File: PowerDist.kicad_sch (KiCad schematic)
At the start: 17 parts, among them J18 PowerConn, Q2 IRLML0030, U12 RI3-1205S, U13 NCP1117-3.3_SOT223

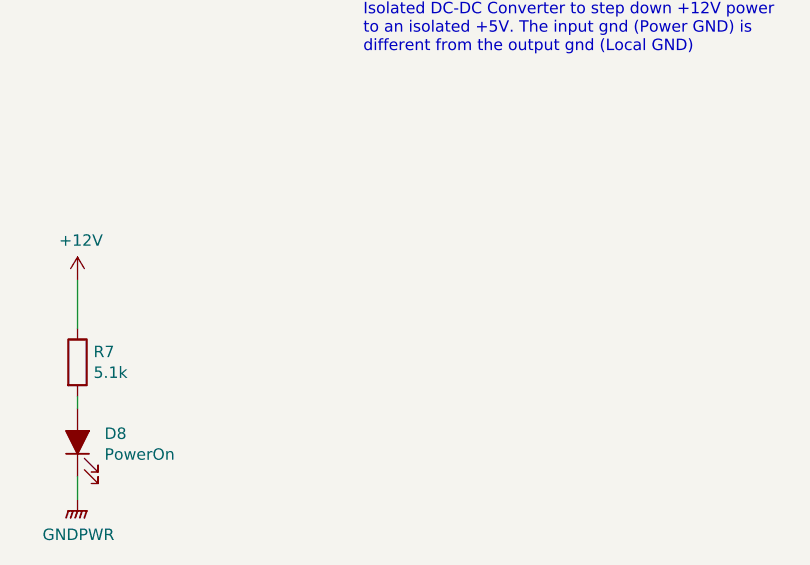
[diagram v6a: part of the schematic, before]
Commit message: Added 3A fuse to lights (estimated 9 lights, ~1.8 A plus buffer, changed fuse datasheet to match part number.
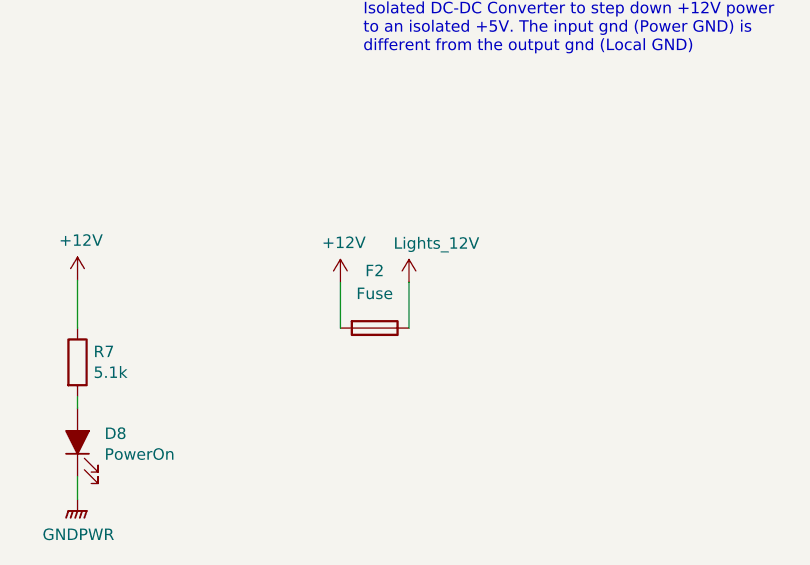
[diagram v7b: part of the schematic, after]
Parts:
- added F2: Fuse, Fuse:Fuse_1206_3216Metric, symbol Device:Fuse
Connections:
- net +12V: now also F2.2
- new net Lights_12V: F2.1
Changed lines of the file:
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@@
+	(wire
+		(pts
+			(xy 96.52 142.24) (xy 96.52 147.32)
+		)
+		(stroke
+			(width 0)
+			(type default)
+		)
+	)
 	(wire
 		(pts
@@
 		(pts
 			(xy 99.06 85.09) (xy 101.6 85.09)
+		)
+		(stroke
+			(width 0)
+			(type default)
+		)
+	)
+	(wire
+		(pts
+			(xy 88.9 142.24) (xy 88.9 147.32)
 		)
 		(stroke
@@
 	)
 	(symbol
+		(lib_id "power:+12V")
+		(at 88.9 142.24 0)
+		(unit 1)
+		(exclude_from_sim no)
+		(in_bom yes)
+		(on_board yes)
+		(dnp no)
+		(property "Reference" "#PWR035"
+			(at 88.9 146.05 0)
+			(effects
+				(font
+					(size 1.27 1.27)
+				)
+				(hide yes)
+			)
+		)
+		(property "Value" "+12V"
+			(at 89.281 137.8458 0)
+			(effects
+				(font
+					(size 1.27 1.27)
+				)
+			)
+		)
+		(property "Footprint" ""
+			(at 88.9 142.24 0)
+			(effects
+				(font
+					(size 1.27 1.27)
+				)
+				(hide yes)
+			)
+		)
+		(property "Datasheet" ""
+			(at 88.9 142.24 0)
+			(effects
+				(font
+					(size 1.27 1.27)
+				)
+				(hide yes)
+			)
+		)
+		(property "Description" "Power symbol creates a global label with name \"+12V\""
+			(at 88.9 142.24 0)
+			(effects
+				(font
+					(size 1.27 1.27)
+				)
+				(hide yes)
+			)
+		)
+		(pin "1"
+		)
+		(instances
+			(project "Controls-Leader"
+				(path "/66218487-e316-4467-9eba-79d4626ab24e/00000000-0000-0000-0000-00005f19a9c5"
+					(reference "#PWR035")
+					(unit 1)
+				)
+			)
+		)
+	)
+	(symbol
 		(lib_id "Diode:SD12_SOD323")
 		(at 55.88 82.55 90)
@@
 				(path "/66218487-e316-4467-9eba-79d4626ab24e/00000000-0000-0000-0000-00005f19a9c5"
 					(reference "TP9")
+					(unit 1)
+				)
+			)
+		)
+	)
+	(symbol
+		(lib_id "Device:Fuse")
+		(at 92.71 147.32 270)
+		(unit 1)
+		(exclude_from_sim no)
+		(in_bom yes)
+		(on_board yes)
+		(dnp no)
+		(fields_autoplaced yes)
+		(property "Reference" "F2"
+			(at 92.71 140.97 90)
+			(effects
+				(font
+					(size 1.27 1.27)
+				)
+			)
+		)
+		(property "Value" "Fuse"
+			(at 92.71 143.51 90)
+			(effects
+				(font
+					(size 1.27 1.27)
+				)
+			)
+		)
+		(property "Footprint" "Fuse:Fuse_1206_3216Metric"
+			(at 92.71 145.542 90)
+			(effects
+				(font
+					(size 1.27 1.27)
+				)
+				(hide yes)
+			)
+		)
+		(property "Datasheet" "https://cdn1-originals.webdamdb.com/14154_151726252?cache=1732578703&response-content-disposition=inline;filename=Littelfuse_Fuse_440_Datasheet.pdf&response-content-type=application/pdf&Policy=eyJTdGF0ZW1lbnQiOlt7IlJlc291cmNlIjoiaHR0cCo6Ly9jZG4xLW9yaWdpbmFscy53ZWJkYW1kYi5jb20vMTQxNTRfMTUxNzI2MjUyP2NhY2hlPTE3MzI1Nzg3MDMmcmVzcG9uc2UtY29udGVudC1kaXNwb3NpdGlvbj1pbmxpbmU7ZmlsZW5hbWU9TGl0dGVsZnVzZV9GdXNlXzQ0MF9EYXRhc2hlZXQucGRmJnJlc3BvbnNlLWNvbnRlbnQtdHlwZT1hcHBsaWNhdGlvbi9wZGYiLCJDb25kaXRpb24iOnsiRGF0ZUxlc3NUaGFuIjp7IkFXUzpFcG9jaFRpbWUiOjIxNDc0MTQ0MDB9fX1dfQ__&Signature=LvuAwZFRA50GgO3enXap8HKIUGPX5c5rkh5wZKPs26l6wVeoa4e3HlPw3JGKu2XLN2mZjekZmdxpYAqdsOFkELgudMCZJJtLLB7CYjilNx-uV0W3LH-UU7j3-UHutrdbGZC827tk~6zJnsDB2xvB98cGEExGU7KZGJANC28jW8XIJPT4hhWJZ3P8A6kmskdfDQHTby0fQLrBki0Cy~JqgrzKU3pon-XdzROvTXY9QwTk8wFP1CPSyVTSOLlxVTny3kR~8QXaPjArNl9XYw9h2m6D9NG~gEpQ45z~3QkwXjtPVVM-Qx0dGMx4oqz-Hj7~vZm16EBMvIaUhjxNWObiWg__&Key-Pair-Id=APKAI2ASI2IOLRFF2RHA"
+			(at 92.71 147.32 0)
+			(effects
+				(font
+					(size 1.27 1.27)
+				)
+				(hide yes)
+			)
+		)
+		(property "Description" "Fuse"
+			(at 92.71 147.32 0)
+			(effects
+				(font
+					(size 1.27 1.27)
+				)
+				(hide yes)
+			)
+		)
+		(property "Id" ""
+			(at 92.71 147.32 0)
+			(effects
+				(font
+					(size 1.27 1.27)
+				)
+				(hide yes)
+			)
+		)
+		(property "Vds" ""
+			(at 92.71 147.32 0)
+			(effects
+				(font
+					(size 1.27 1.27)
+				)
+				(hide yes)
+			)
+		)
+		(property "Mouser Part Number" "576-0440003.WR"
+			(at 92.71 147.32 0)
+			(effects
+				(font
+					(size 1.27 1.27)
+				)
+				(hide yes)
+			)
+		)
+		(pin "2"
+		)
+		(pin "1"
+		)
+		(instances
+			(project "Controls-Leader"
+				(path "/66218487-e316-4467-9eba-79d4626ab24e/00000000-0000-0000-0000-00005f19a9c5"
+					(reference "F2")
 					(unit 1)
 				)
@@
 					(unit 1)
 				)
+			)
+		)
+	)
+	(symbol
+		(lib_id "power:+12V")
+		(at 96.52 142.24 0)
+		(unit 1)
+		(exclude_from_sim no)
+		(in_bom yes)
+		(on_board yes)
+		(dnp no)
+		(property "Reference" "#PWR036"
+			(at 96.52 146.05 0)
+			(effects
+				(font
+					(size 1.27 1.27)
+				)
+				(hide yes)
+			)
+		)
+		(property "Value" "Lights_12V"
+			(at 99.568 137.922 0)
+			(effects
+				(font
+					(size 1.27 1.27)
+				)
+			)
+		)
+		(property "Footprint" ""
+			(at 96.52 142.24 0)
+			(effects
+				(font
+					(size 1.27 1.27)
+				)
+				(hide yes)
+			)
+		)
+		(property "Datasheet" ""
+			(at 96.52 142.24 0)
+			(effects
+				(font
+					(size 1.27 1.27)
+				)
+				(hide yes)
+			)
+		)
+		(property "Description" "Power symbol creates a global label with name \"+12V\""
+			(at 96.52 142.24 0)
+			(effects
+				(font
+					(size 1.27 1.27)
+				)
+				(hide yes)
+			)
+		)
+		(pin "1"
+		)
+		(instances
+			(project "Controls-Leader"
+				(path "/66218487-e316-4467-9eba-79d4626ab24e/00000000-0000-0000-0000-00005f19a9c5"
+					(reference "#PWR036")
+					(unit 1)
+				)

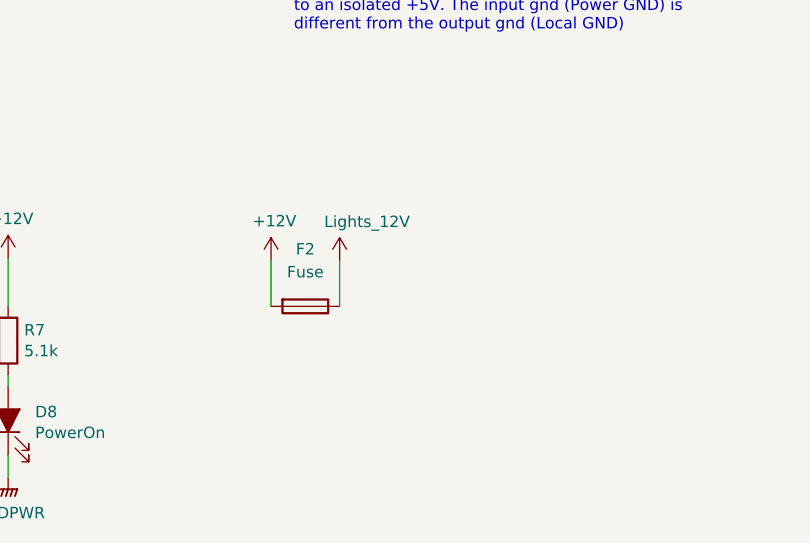
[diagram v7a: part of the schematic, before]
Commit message: Added motor contactor, contactor sense pins, deleted extra GPIO connector 2 since we are now using more of the extra GPIO pins; added new components to layout.
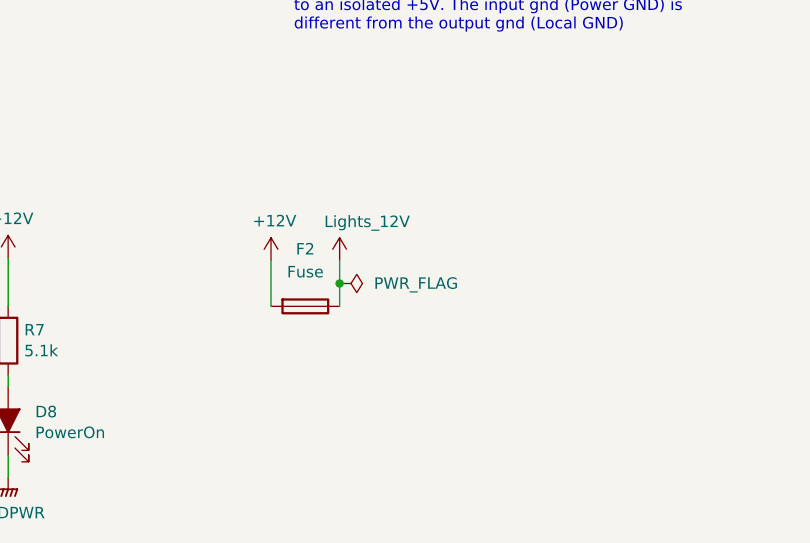
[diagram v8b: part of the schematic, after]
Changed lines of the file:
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@@
 	)
 	(junction
+		(at 96.52 144.78)
+		(diameter 0)
+		(color 0 0 0 0)
+	)
+	(junction
 		(at 43.18 81.28)
 		(diameter 0)
@@
 	(wire
 		(pts
+			(xy 96.52 144.78) (xy 96.52 147.32)
+		)
+		(stroke
+			(width 0)
+			(type default)
+		)
+	)
+	(wire
+		(pts
 			(xy 85.09 77.47) (xy 85.09 80.01)
 		)
@@
 	(wire
 		(pts
-			(xy 96.52 142.24) (xy 96.52 147.32)
+			(xy 96.52 142.24) (xy 96.52 144.78)
 		)
 		(stroke
@@
 					(unit 1)
 				)
+			)
+		)
+	)
+	(symbol
+		(lib_id "power:PWR_FLAG")
+		(at 96.52 144.78 270)
+		(unit 1)
+		(exclude_from_sim no)
+		(in_bom yes)
+		(on_board yes)
+		(dnp no)
+		(fields_autoplaced yes)
+		(property "Reference" "#FLG03"
+			(at 98.425 144.78 0)
+			(effects
+				(font
+					(size 1.27 1.27)
+				)
+				(hide yes)
+			)
+		)
+		(property "Value" "PWR_FLAG"
+			(at 100.33 144.7799 90)
+			(effects
+				(font
+					(size 1.27 1.27)
+				)
+				(justify left)
+			)
+		)
+		(property "Footprint" ""
+			(at 96.52 144.78 0)
+			(effects
+				(font
+					(size 1.27 1.27)
+				)
+				(hide yes)
+			)
+		)
+		(property "Datasheet" "~"
+			(at 96.52 144.78 0)
+			(effects
+				(font
+					(size 1.27 1.27)
+				)
+				(hide yes)
+			)
+		)
+		(property "Description" "Special symbol for telling ERC where power comes from"
+			(at 96.52 144.78 0)
+			(effects
+				(font
+					(size 1.27 1.27)
+				)
+				(hide yes)
+			)
+		)
+		(pin "1"
+		)
+		(instances
+			(project ""
+				(path "/66218487-e316-4467-9eba-79d4626ab24e/00000000-0000-0000-0000-00005f19a9c5"
+					(reference "#FLG03")
+					(unit 1)
+				)
